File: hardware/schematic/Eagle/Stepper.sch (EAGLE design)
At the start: 38 parts, among them U16 MMSZ5225BT1G, U19 LM358DR

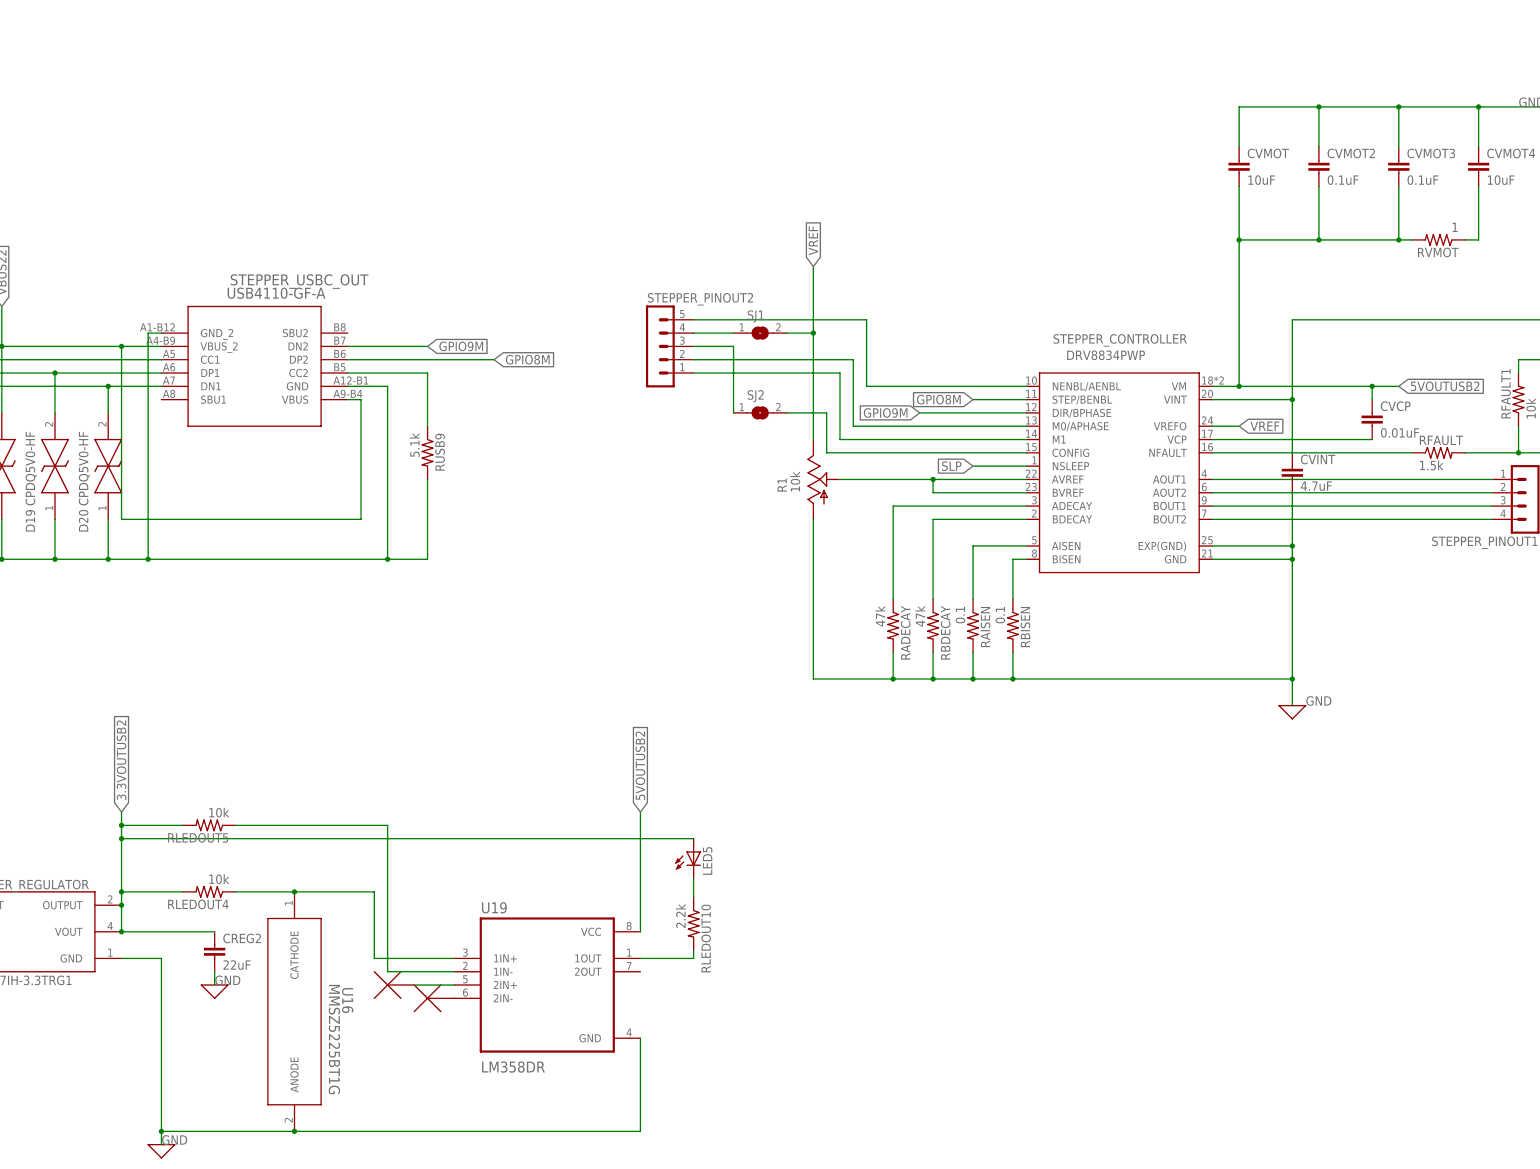
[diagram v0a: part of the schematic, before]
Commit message: updated with Dr.Week's advice
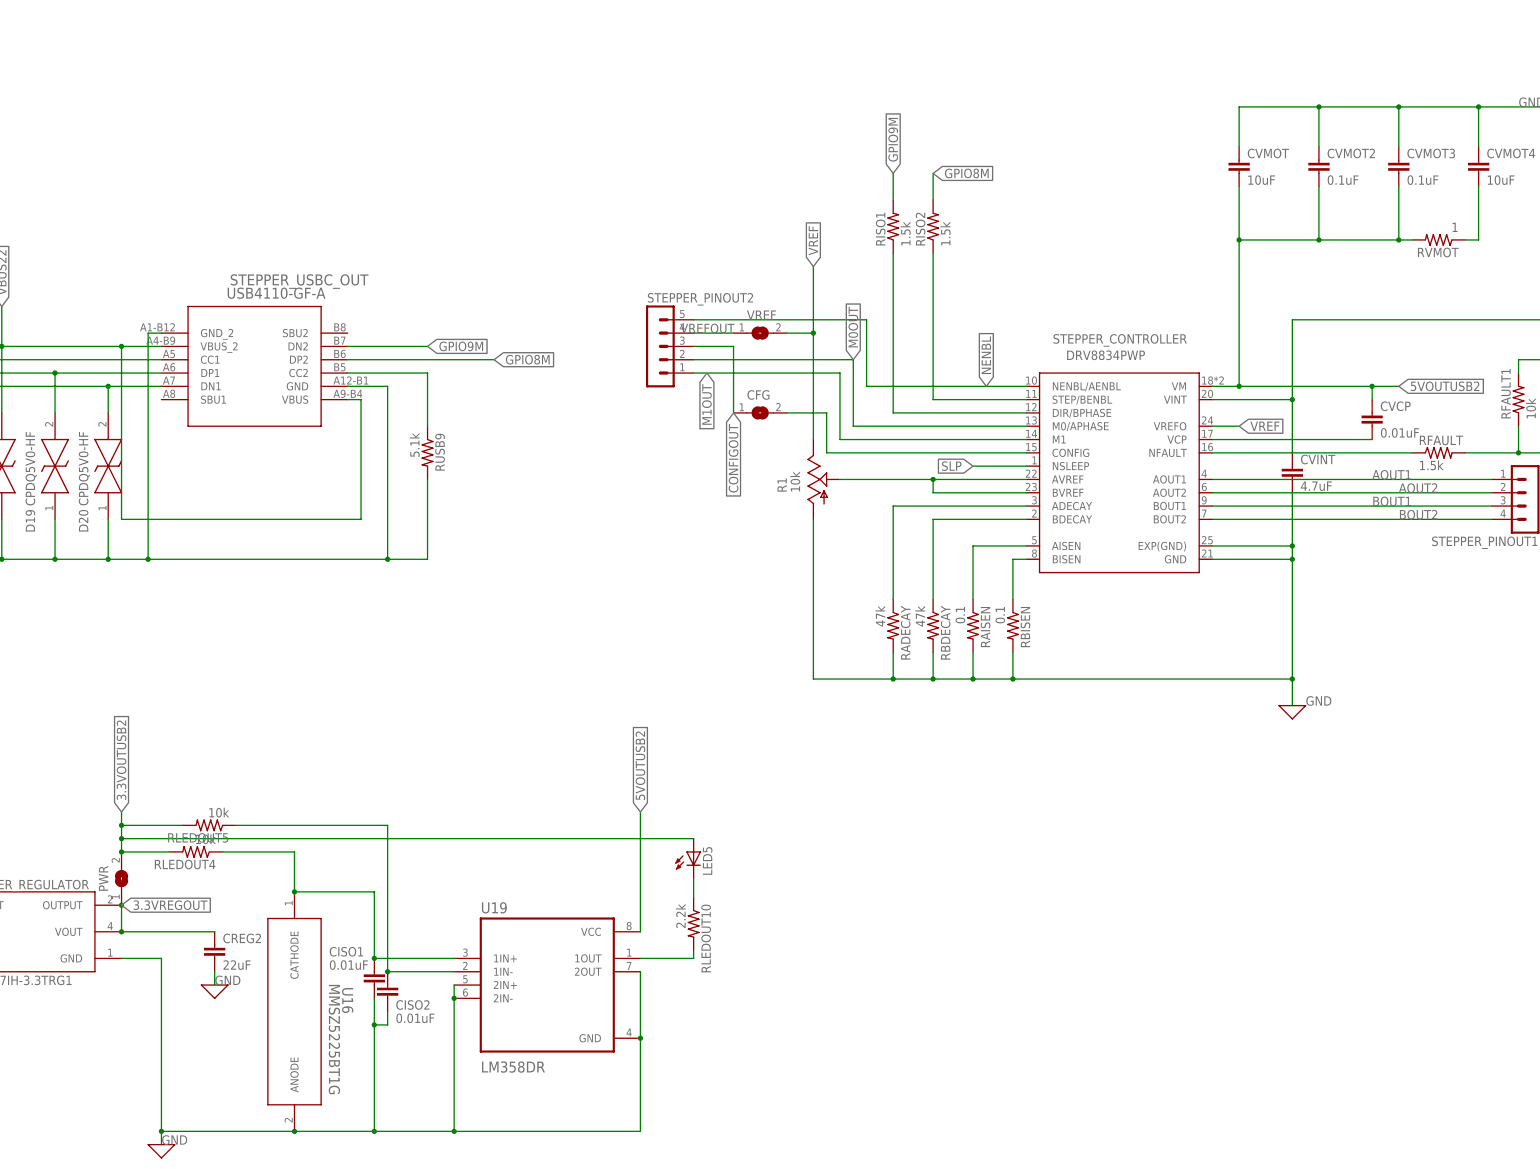
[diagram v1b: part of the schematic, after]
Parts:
- removed U$8, U$9: NC_MARKER, NC_MARKER:NC_MARKER
- added CISO1, CISO2: 0.01uF, rcl:C-EUC0805
- added PWR: (no value), jumper:SJ
- added RISO1, RISO2: 1.5k, rcl:R-US_M0805
- renumbered SJ1 to VREF, SJ2 to CFG
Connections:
- net N$28 renamed AOUT1
- net N$29 renamed AOUT2
- net N$30 renamed BOUT1
- net N$31 renamed BOUT2
- net N$34 renamed VREFOUT
- net N$35 renamed CONFIGOUT
- net N$37 renamed M1OUT
- net N$38 renamed M0OUT
- net N$90 renamed NENBL
- removed net N$87: U$9.P$1, U19.2IN-
- removed net N$89: U$8.P$1, U19.2IN+
- new net 3.3VREGOUT: CREG2.1, PWR.1, STEPPER_REGULATOR.OUTPUT, STEPPER_REGULATOR.VOUT
- new net N$1: RISO1.1, STEPPER_CONTROLLER.DIR/BPHASE
- new net N$2: RISO2.1, STEPPER_CONTROLLER.STEP/BENBL
- net 3.3VOUTUSB2: now also PWR.2; no longer CREG2.1, STEPPER_REGULATOR.OUTPUT, STEPPER_REGULATOR.VOUT
- net GND: now also CISO1.2, CISO2.2, U19.2IN+, U19.2IN-, U19.2OUT
- net GPIO8M: now also RISO2.2; no longer STEPPER_CONTROLLER.STEP/BENBL
- net GPIO9M: now also RISO1.2; no longer STEPPER_CONTROLLER.DIR/BPHASE
- net N$82: now also CISO1.1
- net N$83: now also CISO2.1
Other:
- moved on the sheet: RLEDOUT4
